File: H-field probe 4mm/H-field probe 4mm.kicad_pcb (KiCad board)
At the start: 4 copper layers, 62.8 x 12 mm, 1 part, among them J1 Conn_Coaxial

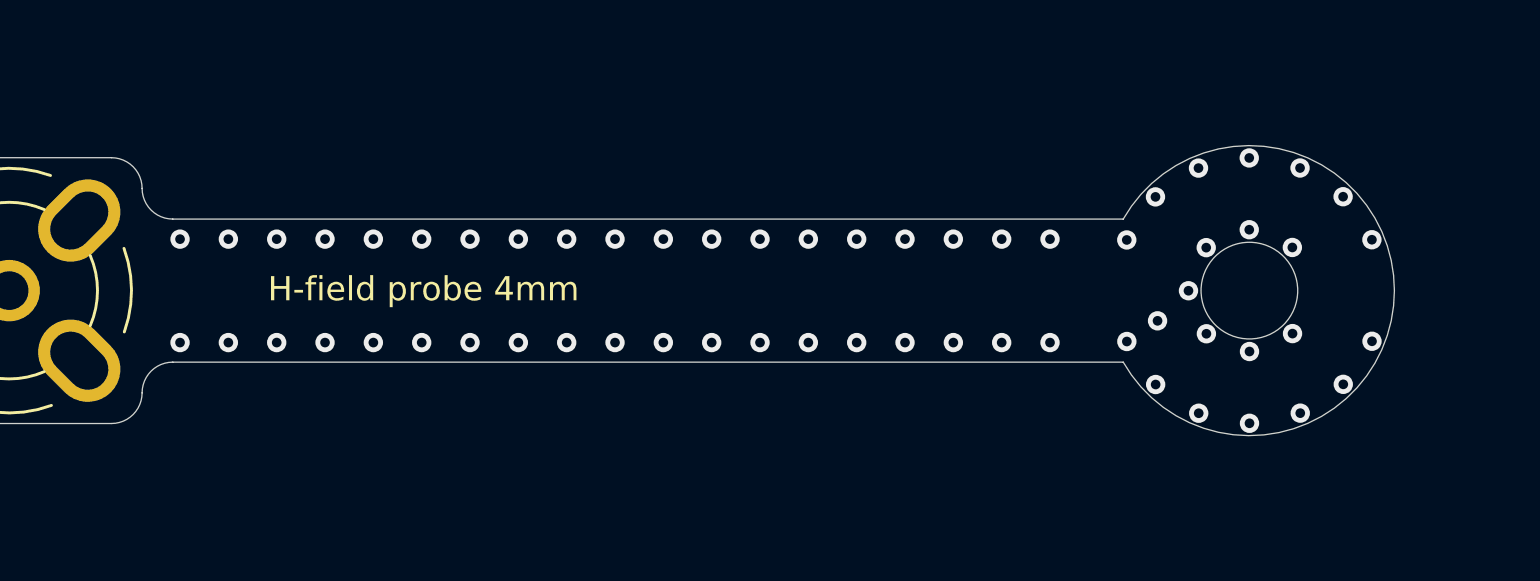
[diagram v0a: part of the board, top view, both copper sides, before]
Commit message: Fixed wrong diamter. Changed via size. Added text and logo
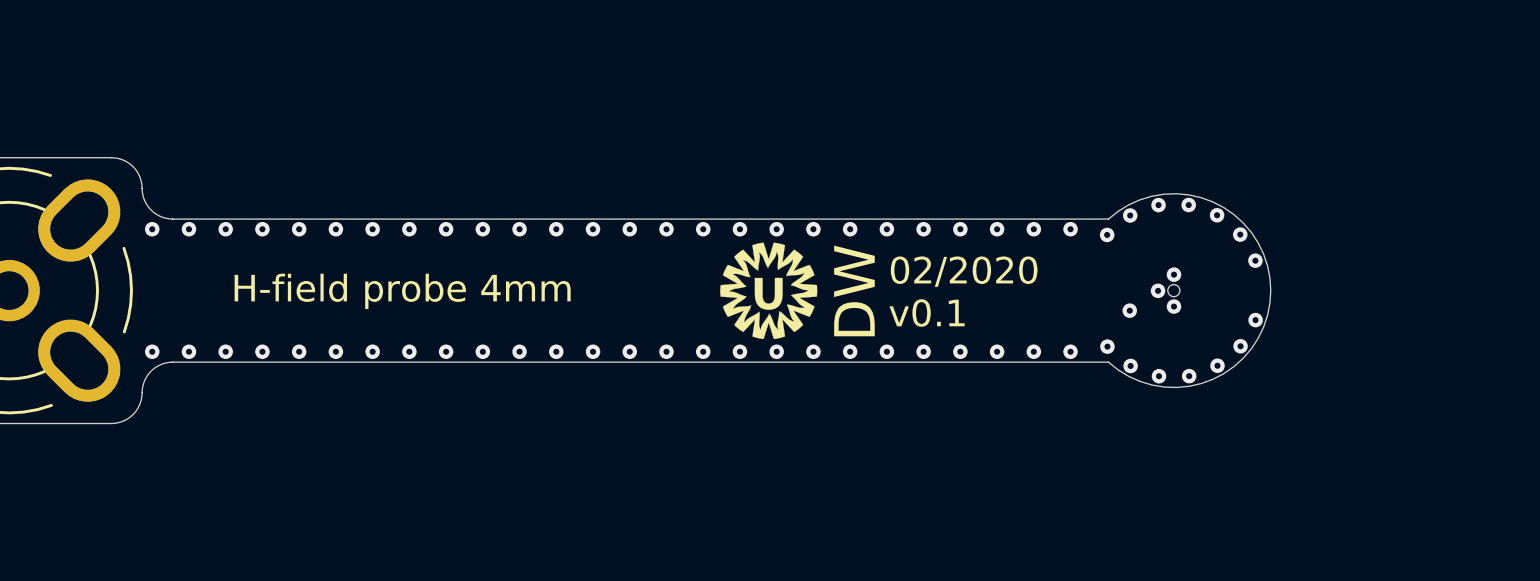
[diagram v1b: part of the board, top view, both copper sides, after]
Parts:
- added G***: LOGO, _Custom:UMC_logo_4mm, F.Cu at (142.3, 96.3)
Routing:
- net Net-(J1-Pad1): track 47.3 -> 46.2 mm
- net GND: vias 60 -> 70
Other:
- board size 62.8 x 12 mm -> 57.7 x 11 mm
- rule via_min_drill: 0.3 -> 0.25
- board text added: "02/2020 v0.1"
- board text added: "DW"

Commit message: Updated connector
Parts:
- turned J1 to 270 degrees
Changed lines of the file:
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@@
     (add_net "Net-(J1-Pad1)")
+  )
+  (module _Custom:BNC_SMA_Vertical (layer F.Cu)
+    (at 110.88 96.27 270)
+    (descr "BNC female PCB mount 4 pin straight chassis connector http://www.te.com/usa-en/product-1-1478204-0.html")
+    (tags "BNC female PCB mount 4 pin straight chassis connector ")
+    (fp_text reference J1 (at -4.32 0) (layer F.SilkS) hide
+      (effects (font (size 1 1) (thickness 0.15)))
+    )
+    (fp_text value Conn_Coaxial (at 0 6.5 90) (layer F.Fab)
+      (effects (font (size 1 1) (thickness 0.15)))
+    )
+    (fp_line (start -2.54 5.08) (end 2.54 5.08) (layer F.SilkS) (width 0.12))
+    (fp_text user %R (at 0 0 90) (layer F.Fab)
+      (effects (font (size 1 1) (thickness 0.15)))
+    )
+    (fp_line (start 5.5 -5.5) (end 5.5 5.5) (layer F.CrtYd) (width 0.05))
+    (fp_line (start 5.5 5.5) (end -5.5 5.5) (layer F.CrtYd) (width 0.05))
+    (fp_line (start -5.5 5.5) (end -5.5 -5.5) (layer F.CrtYd) (width 0.05))
+    (fp_line (start -5.5 -5.5) (end 5.5 -5.5) (layer F.CrtYd) (width 0.05))
+    (fp_circle (center 0 0) (end 4.8 0) (layer F.Fab) (width 0.1))
+    (fp_arc (start 0 0) (end -4.75 1.75) (angle 40) (layer F.SilkS) (width 0.12))
+    (fp_arc (start 0 0) (end 4.75 -1.75) (angle 40) (layer F.SilkS) (width 0.12))
+    (fp_arc (start 0 0) (end -1.75 -4.75) (angle 40) (layer F.SilkS) (width 0.12))
+    (fp_circle (center 0 0) (end 3.175 0) (layer F.Fab) (width 0.1))
+    (fp_arc (start 0 0) (end 3.355 -1.45) (angle 46.74710926) (layer F.SilkS) (width 0.12))
+    (fp_arc (start 0 0) (end -3.355 1.45) (angle 46.74710926) (layer F.SilkS) (width 0.12))
+    (fp_arc (start 0 0) (end -1.45 -3.355) (angle 46.74710926) (layer F.SilkS) (width 0.12))
+    (fp_arc (start 0 0) (end 1.45 3.355) (angle 46.74710926) (layer F.SilkS) (width 0.12))
+    (pad 2 thru_hole oval (at -2.9 -2.9 315) (size 2.7 3.7) (drill oval 1.7 2.7) (layers *.Cu *.Mask)
+      (net 2 GND))
+    (pad 1 thru_hole circle (at 0 0 270) (size 2.54 2.54) (drill 1.6) (layers *.Cu *.Mask)
+      (net 1 "Net-(J1-Pad1)"))
+    (pad 2 thru_hole oval (at 2.9 -2.9 225) (size 2.7 3.7) (drill oval 1.7 2.7) (layers *.Cu *.Mask)
+      (net 2 GND))
+    (pad 2 thru_hole oval (at -2.9 2.9 225) (size 2.7 3.7) (drill oval 1.7 2.7) (layers *.Cu *.Mask)
+      (net 2 GND))
+    (pad 2 thru_hole oval (at 2.9 2.9 315) (size 2.7 3.7) (drill oval 1.7 2.7) (layers *.Cu *.Mask)
+      (net 2 GND))
+    (model :_Custom_3D:BNC_73171-3356.stp
+      (offset (xyz 0 -22.7 6.1))
+      (scale (xyz 1 1 1))
+      (rotate (xyz -90 0 0))
+    )
   )
   (module _Custom:UMC_logo_4mm (layer F.Cu)
@@
       (xy -0.572109 -0.154103) (xy -0.573425 -0.53278) (xy -0.257097 -0.53278) (xy -0.257071 -0.169591)) (layer F.SilkS) (width 0.01))
   )
-  (module _Custom:BNC_SMA_Vertical (layer F.Cu)
-    (at 110.88 96.27)
-    (descr "BNC female PCB mount 4 pin straight chassis connector http://www.te.com/usa-en/product-1-1478204-0.html")
-    (tags "BNC female PCB mount 4 pin straight chassis connector ")
-    (fp_text reference J1 (at -4.32 0 90) (layer F.SilkS) hide
-      (effects (font (size 1 1) (thickness 0.15)))
-    )
-    (fp_text value Conn_Coaxial (at 0 6.5) (layer F.Fab)
-      (effects (font (size 1 1) (thickness 0.15)))
-    )
-    (fp_arc (start 0 0) (end 1.45 3.355) (angle 46.74710926) (layer F.SilkS) (width 0.12))
-    (fp_arc (start 0 0) (end -1.45 -3.355) (angle 46.74710926) (layer F.SilkS) (width 0.12))
-    (fp_arc (start 0 0) (end -3.355 1.45) (angle 46.74710926) (layer F.SilkS) (width 0.12))
-    (fp_arc (start 0 0) (end 3.355 -1.45) (angle 46.74710926) (layer F.SilkS) (width 0.12))
-    (fp_circle (center 0 0) (end 3.175 0) (layer F.Fab) (width 0.1))
-    (fp_arc (start 0 0) (end -1.75 -4.75) (angle 40) (layer F.SilkS) (width 0.12))
-    (fp_arc (start 0 0) (end 4.75 -1.75) (angle 40) (layer F.SilkS) (width 0.12))
-    (fp_arc (start 0 0) (end 1.75 4.75) (angle 40) (layer F.SilkS) (width 0.12))
-    (fp_arc (start 0 0) (end -4.75 1.75) (angle 40) (layer F.SilkS) (width 0.12))
-    (fp_circle (center 0 0) (end 4.8 0) (layer F.Fab) (width 0.1))
-    (fp_line (start -5.5 -5.5) (end 5.5 -5.5) (layer F.CrtYd) (width 0.05))
-    (fp_line (start -5.5 5.5) (end -5.5 -5.5) (layer F.CrtYd) (width 0.05))
-    (fp_line (start 5.5 5.5) (end -5.5 5.5) (layer F.CrtYd) (width 0.05))
-    (fp_line (start 5.5 -5.5) (end 5.5 5.5) (layer F.CrtYd) (width 0.05))
-    (fp_text user %R (at 0 0) (layer F.Fab)
-      (effects (font (size 1 1) (thickness 0.15)))
-    )
-    (pad 2 thru_hole oval (at 2.9 2.9 45) (size 2.7 3.7) (drill oval 1.7 2.7) (layers *.Cu *.Mask)
-      (net 2 GND))
-    (pad 2 thru_hole oval (at -2.9 2.9 315) (size 2.7 3.7) (drill oval 1.7 2.7) (layers *.Cu *.Mask)
-      (net 2 GND))
-    (pad 2 thru_hole oval (at 2.9 -2.9 315) (size 2.7 3.7) (drill oval 1.7 2.7) (layers *.Cu *.Mask)
-      (net 2 GND))
-    (pad 1 thru_hole circle (at 0 0) (size 2.54 2.54) (drill 1.6) (layers *.Cu *.Mask)
-      (net 1 "Net-(J1-Pad1)") (clearance 0.2))
-    (pad 2 thru_hole oval (at -2.9 -2.9 45) (size 2.7 3.7) (drill oval 1.7 2.7) (layers *.Cu *.Mask)
-      (net 2 GND))
-    (model ${KISYS3DMOD}/Connector_Coaxial.3dshapes/BNC_TEConnectivity_1478204_Vertical.wrl
-      (at (xyz 0 0 0))
-      (scale (xyz 1 1 1))
-      (rotate (xyz 0 0 0))
-    )
-  )
   (gr_circle (center 159.075 96.27) (end 159.325 96.27) (layer Edge.Cuts) (width 0.01))
